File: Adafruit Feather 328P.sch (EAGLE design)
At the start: 39 parts, among them IC1 CP2104, IC2 ATMEGA328P, Q3 DMG341, SW2 KMR2, U2 AP2112-3.3, U3 MCP73831T-2ACI/OT, X1 JSTPH, X4 20329, Y2 CSTCE16M0V53-R0 8MHZ

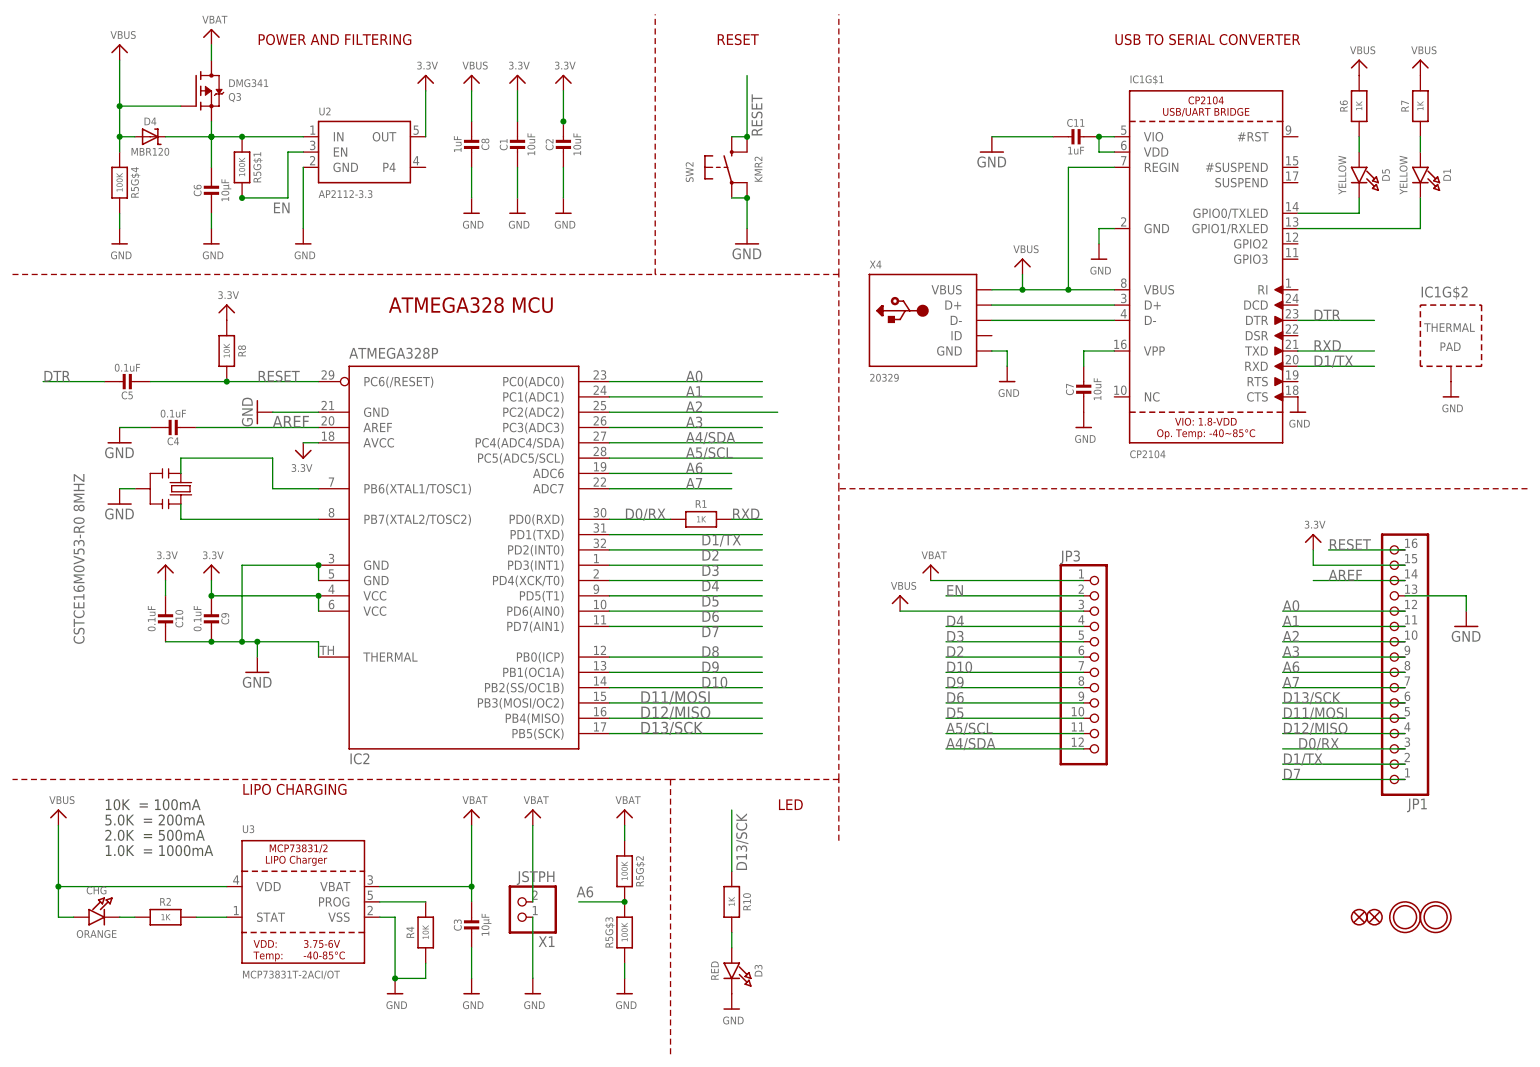
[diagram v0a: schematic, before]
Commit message: fix https://github.com/adafruit/Adafruit-Feather-328P-PCB/issues/2
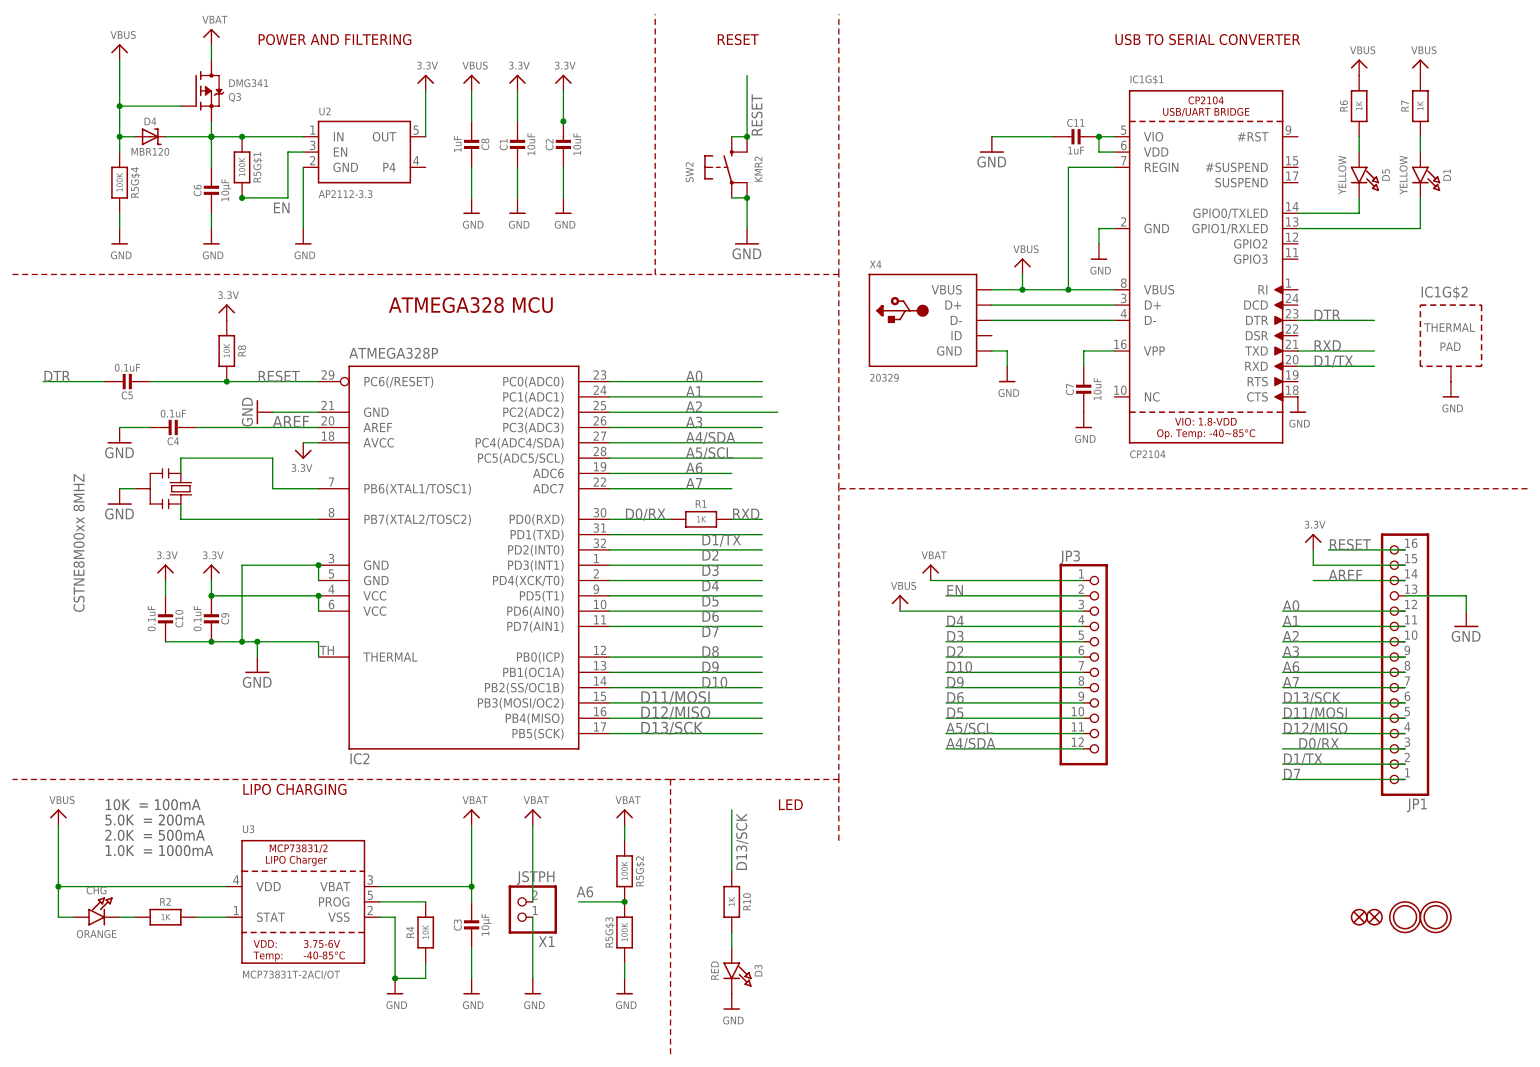
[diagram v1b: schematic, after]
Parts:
- Y2: value CSTCE16M0V53-R0 8MHZ -> CSTNE8M00xx 8MHZ
